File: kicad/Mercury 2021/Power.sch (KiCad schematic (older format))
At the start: 27 parts, among them J1 Batt_Power, J10 3.3v rail, J11 Screw_Terminal_01x02, J12 Screw_Terminal_01x02, J13 Screw_Terminal_01x02, J14 Screw_Terminal_01x02, J2 Screw_Terminal_01x02, J3 Screw_Terminal_01x02, J30 Screw_Terminal_01x02, J31 Screw_Terminal_01x02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

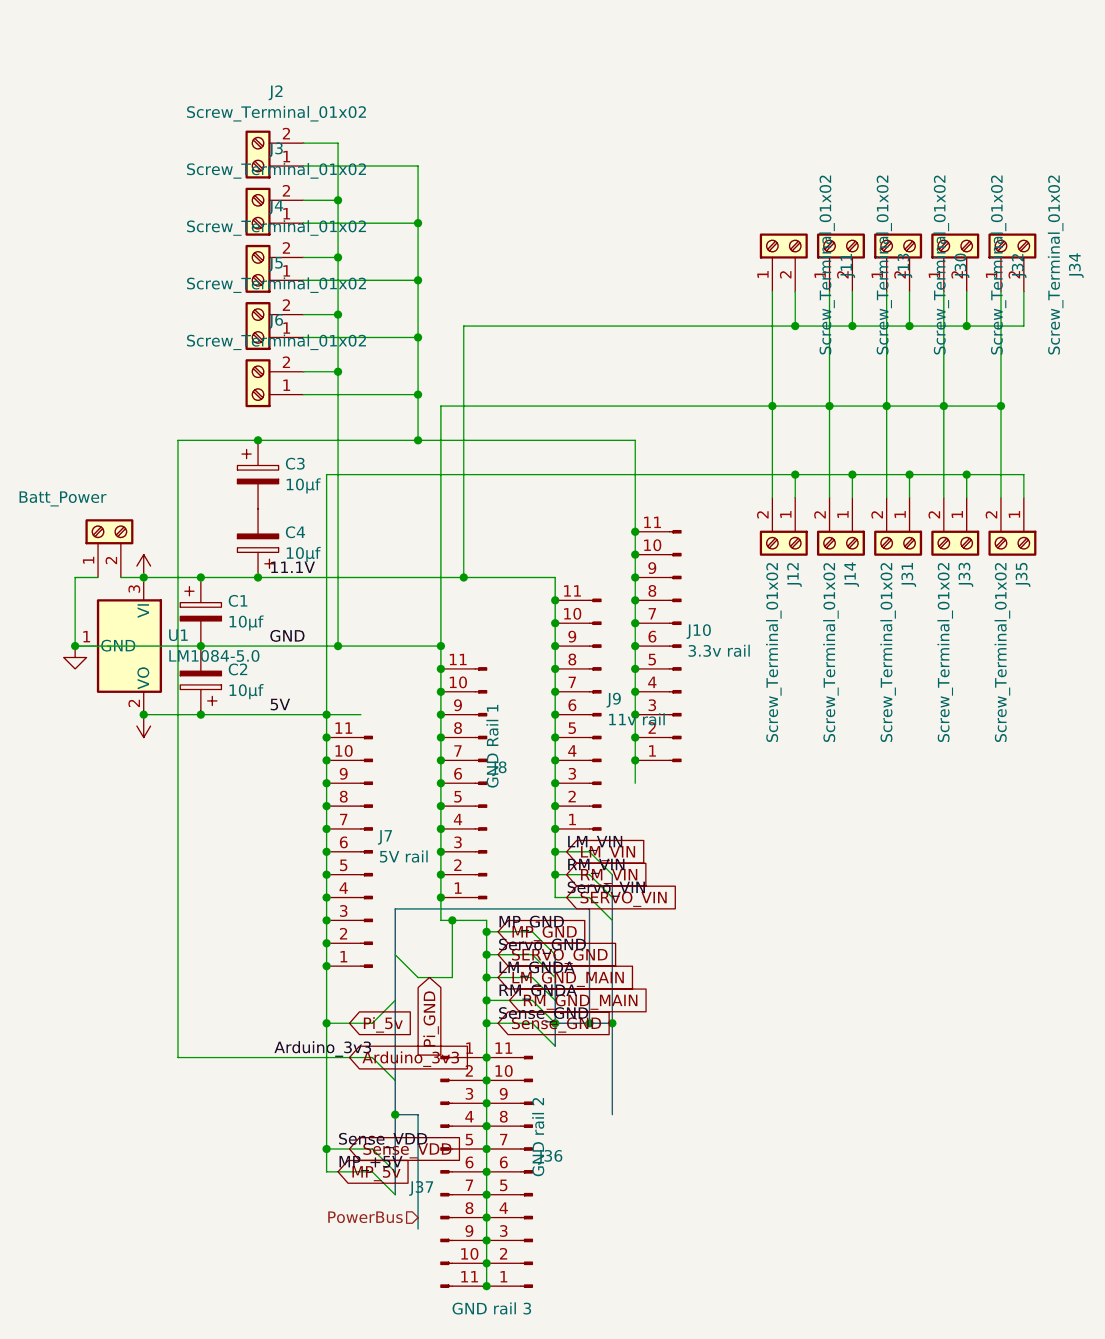
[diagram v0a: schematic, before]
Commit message: Updated new board
- Did PCB traces
-- almost got away with just 2 copper layers, pi ruined it when there was only a bit to go. Probably possible but would take a lot of back and forth
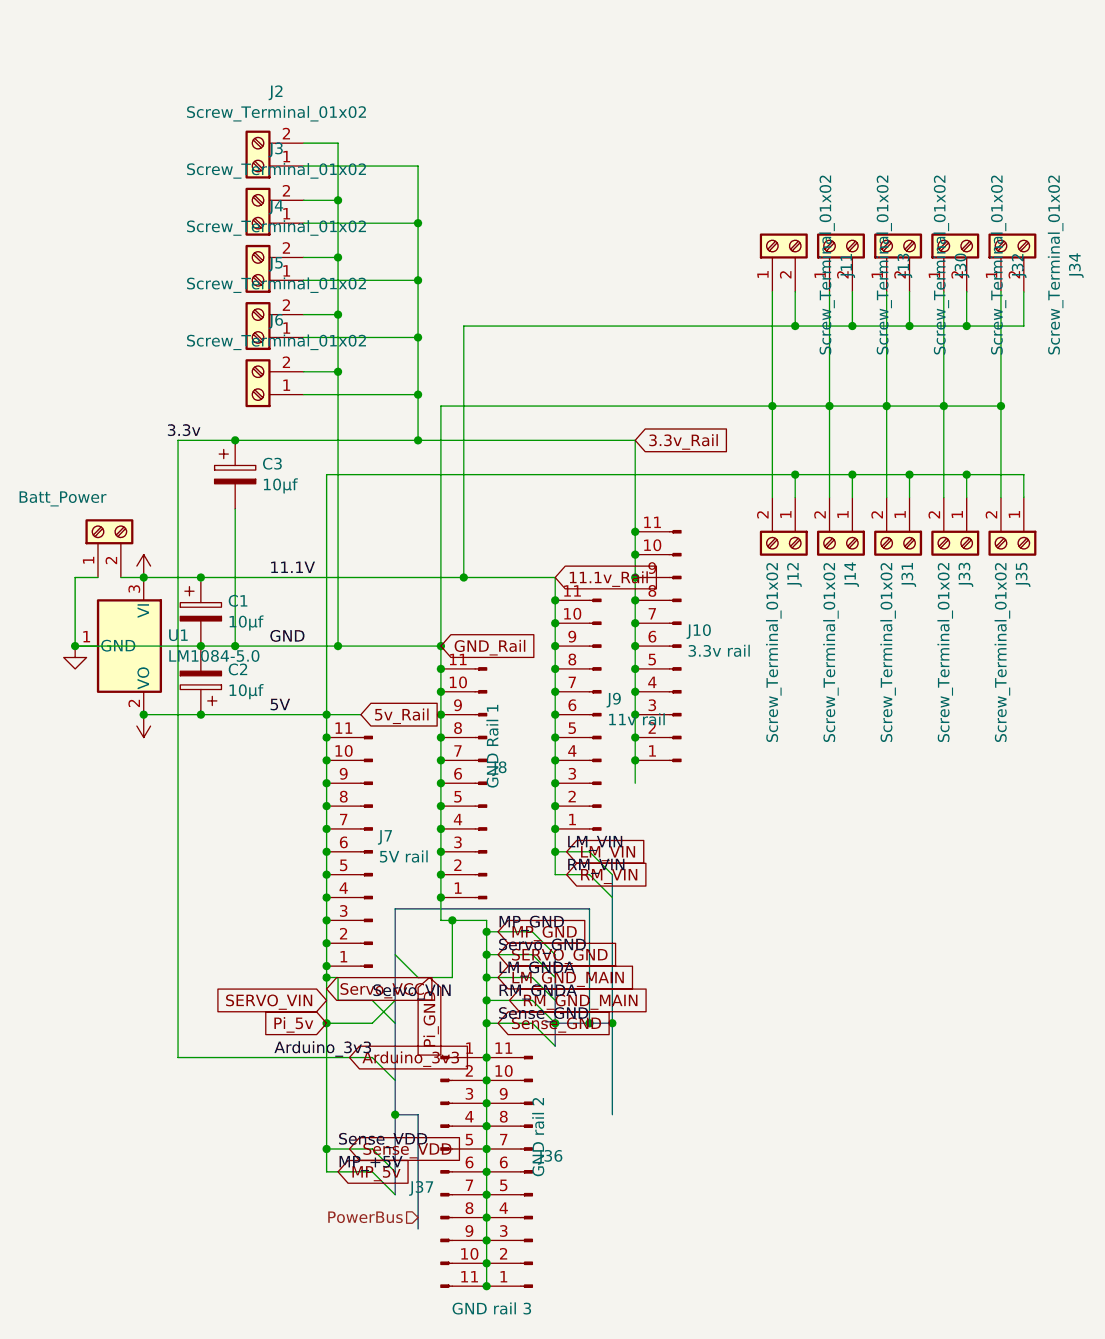
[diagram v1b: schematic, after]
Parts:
- removed C4: 10μf, Capacitor_THT:CP_Radial_D10.0mm_P2.50mm, symbol Device:CP
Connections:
- net GND: now also C3.2
- net Arduino_3v3 renamed 3.3v_Rail
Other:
- moved on the sheet: C3
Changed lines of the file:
@@
 Connection ~ 3450 3850
 Wire Wire Line
-	3450 3850 4050 3850
+	3450 3850 3600 3850
 $Comp
 L Connector:Screw_Terminal_01x02 J?
@@
 	5150 4850 5250 4950
 Entry Wire Line
-	5150 4950 5250 5050
+	4200 5400 4300 5500
 Wire Wire Line
 	5000 4850 5150 4850
 Wire Wire Line
-	5000 4950 5150 4950
+	4050 5400 4200 5400
 Wire Wire Line
 	5000 4750 5150 4750
 Text Label 5050 4850 0    50   ~ 0
 RM_VIN
-Text Label 5050 4950 0    50   ~ 0
-Servo_VIN
 Text Label 5050 4750 0    50   ~ 0
 LM_VIN
@@
 	5000 4750 5000 4850
 Wire Wire Line
-	5000 4850 5000 4950
-Connection ~ 5000 4850
+	4050 5300 4050 5400
 Wire Bus Line
 	4400 6400 4400 5900
@@
 	-1   0    0    1
 $EndComp
-Wire Wire Line
-	3450 3550 3700 3550
-$Comp
-L Device:CP C?
-U 1 1 60EA6068
-P 3700 3400
-AR Path="/60EA6068" Ref="C?"  Part="1"
-AR Path="/60E98AAB/60EA6068" Ref="C4"  Part="1"
-F 0 "C4" H 3582 3354 50  0000 R CNN
-F 1 "10μf" H 3582 3445 50  0000 R CNN
-F 2 "Capacitor_THT:CP_Radial_D10.0mm_P2.50mm" H 3738 3250 50  0001 C CNN
-F 3 "~" H 3700 3400 50  0001 C CNN
-	1    3700 3400
-	-1   0    0    1
-$EndComp
 $Comp
 L Device:CP C?
 U 1 1 60EA606E
-P 3700 3100
+P 3600 3100
 AR Path="/60EA606E" Ref="C?"  Part="1"
 AR Path="/60E98AAB/60EA606E" Ref="C3"  Part="1"
-F 0 "C3" H 3818 3146 50  0000 L CNN
-F 1 "10μf" H 3818 3055 50  0000 L CNN
-F 2 "Capacitor_THT:CP_Radial_D10.0mm_P2.50mm" H 3738 2950 50  0001 C CNN
-F 3 "~" H 3700 3100 50  0001 C CNN
-	1    3700 3100
+F 0 "C3" H 3718 3146 50  0000 L CNN
+F 1 "10μf" H 3718 3055 50  0000 L CNN
+F 2 "Capacitor_THT:CP_Radial_D10.0mm_P2.50mm" H 3638 2950 50  0001 C CNN
+F 3 "~" H 3600 3100 50  0001 C CNN
+	1    3600 3100
 	1    0    0    -1
 $EndComp
@@
 Wire Wire Line
 	3450 4150 4000 4150
-Connection ~ 3700 3550
-Wire Wire Line
-	3700 3550 4600 3550
-Wire Wire Line
-	3350 2950 3700 2950
-Connection ~ 3700 2950
+Wire Wire Line
+	3350 2950 3600 2950
 Connection ~ 5350 3650
 $Comp
@@
 Connection ~ 4400 2950
 Connection ~ 4050 3850
-Wire Wire Line
-	3700 2950 4400 2950
 Wire Wire Line
 	4050 2650 4050 3850
@@
 Text GLabel 5050 4850 2    50   Input ~ 0
 RM_VIN
-Text GLabel 5050 4950 2    50   Input ~ 0
+Text GLabel 4000 5400 0    50   Input ~ 0
 SERVO_VIN
 Text GLabel 4100 6050 2    50   Input ~ 0
@@
 MP_5v
 Wire Wire Line
-	4000 5250 4000 5500
+	4000 5250 4000 5300
 Text GLabel 4100 5650 2    50   Input ~ 0
 Arduino_3v3
-Text GLabel 4100 5500 2    50   Input ~ 0
+Text GLabel 4000 5500 0    50   Input ~ 0
 Pi_5v
 Text GLabel 4450 5300 3    50   Input ~ 0
@@
 Wire Wire Line
 	4550 5300 4400 5300
+Connection ~ 4550 5050
+Wire Wire Line
+	4550 5050 4700 5050
+Text Label 3450 2950 2    50   ~ 0
+3.3v
+Text GLabel 5350 2950 2    50   Input ~ 0
+3.3v_Rail
+Text GLabel 5000 3550 2    50   Input ~ 0
+11.1v_Rail
+Text GLabel 4500 3850 2    50   Input ~ 0
+GND_Rail
+Text GLabel 4150 4150 2    50   Input ~ 0
+5v_Rail
+Connection ~ 3600 2950
+Wire Wire Line
+	3600 3250 3600 3850
+Wire Wire Line
+	3600 2950 4400 2950
+Connection ~ 3600 3850
+Wire Wire Line
+	3600 3850 4050 3850
+Wire Wire Line
+	3450 3550 4600 3550
+Text GLabel 4000 5350 2    50   Input ~ 0
+Servo_VCC
+Text Label 4200 5400 0    50   ~ 0
+Servo_VIN
+Wire Wire Line
+	4050 5300 4000 5300
 Wire Bus Line
 	4300 5900 4300 6250
@@
 Wire Bus Line
 	4300 5000 4300 5900
-Connection ~ 4550 5050
-Wire Wire Line
-	4550 5050 4700 5050
+Connection ~ 4000 5300
+Wire Wire Line
+	4000 5300 4000 5500
 $EndSCHEMATC

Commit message: New New board
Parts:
- removed C3: 10μf, Capacitor_THT:CP_Radial_D10.0mm_P2.50mm, symbol Device:CP
- removed J11, J12, J2, J3, J34, J35, J6: Screw_Terminal_01x02, TerminalBlock:TerminalBlock_Altech_AK300-2_P5.00mm, symbol Connector:Screw_Terminal_01x02
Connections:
- wire segments 162 -> 139
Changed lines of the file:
@@
-$Comp
-L Connector:Screw_Terminal_01x02 J?
-U 1 1 60EA5FEE
-P 6050 3400
-AR Path="/60EA5FEE" Ref="J?"  Part="1"
-AR Path="/60E98AAB/60EA5FEE" Ref="J12"  Part="1"
-F 0 "J12" H 6130 3392 50  0000 L CNN
-F 1 "Screw_Terminal_01x02" H 6130 3301 50  0000 L CNN
-F 2 "TerminalBlock:TerminalBlock_Altech_AK300-2_P5.00mm" H 6050 3400 50  0001 C CNN
-F 3 "~" H 6050 3400 50  0001 C CNN
-	1    6050 3400
-	0    1    1    0
-$EndComp
 $Comp
 L Connector:Screw_Terminal_01x02 J?
@@
 $Comp
 L Connector:Screw_Terminal_01x02 J?
-U 1 1 60EA6006
-P 7050 3400
-AR Path="/60EA6006" Ref="J?"  Part="1"
-AR Path="/60E98AAB/60EA6006" Ref="J35"  Part="1"
-F 0 "J35" H 7130 3392 50  0000 L CNN
-F 1 "Screw_Terminal_01x02" H 7130 3301 50  0000 L CNN
-F 2 "TerminalBlock:TerminalBlock_Altech_AK300-2_P5.00mm" H 7050 3400 50  0001 C CNN
-F 3 "~" H 7050 3400 50  0001 C CNN
-	1    7050 3400
-	0    1    1    0
-$EndComp
-$Comp
-L Connector:Screw_Terminal_01x02 J?
-U 1 1 60EA600C
-P 6950 2100
-AR Path="/60EA600C" Ref="J?"  Part="1"
-AR Path="/60E98AAB/60EA600C" Ref="J34"  Part="1"
-F 0 "J34" H 6868 1775 50  0000 C CNN
-F 1 "Screw_Terminal_01x02" H 6868 1866 50  0000 C CNN
-F 2 "TerminalBlock:TerminalBlock_Altech_AK300-2_P5.00mm" H 6950 2100 50  0001 C CNN
-F 3 "~" H 6950 2100 50  0001 C CNN
-	1    6950 2100
-	0    -1   -1   0
-$EndComp
-$Comp
-L Connector:Screw_Terminal_01x02 J?
 U 1 1 60EA6012
 P 6700 2100
@@
 AR Path="/60E98AAB/60EA6012" Ref="J32"  Part="1"
 F 0 "J32" H 6618 1775 50  0000 C CNN
-F 1 "Screw_Terminal_01x02" H 6618 1866 50  0000 C CNN
+F 1 "Screw_Terminal_01x02" H 7050 1900 50  0000 C CNN
 F 2 "TerminalBlock:TerminalBlock_Altech_AK300-2_P5.00mm" H 6700 2100 50  0001 C CNN
 F 3 "~" H 6700 2100 50  0001 C CNN
@@
 AR Path="/60E98AAB/60EA6018" Ref="J30"  Part="1"
 F 0 "J30" H 6368 1775 50  0000 C CNN
-F 1 "Screw_Terminal_01x02" H 6368 1866 50  0000 C CNN
+F 1 "Screw_Terminal_01x02" H 6950 1850 50  0000 C CNN
 F 2 "TerminalBlock:TerminalBlock_Altech_AK300-2_P5.00mm" H 6450 2100 50  0001 C CNN
 F 3 "~" H 6450 2100 50  0001 C CNN
 	1    6450 2100
-	0    -1   -1   0
-$EndComp
-$Comp
-L Connector:Screw_Terminal_01x02 J?
-U 1 1 60EA601E
-P 6200 2100
-AR Path="/60EA601E" Ref="J?"  Part="1"
-AR Path="/60E98AAB/60EA601E" Ref="J13"  Part="1"
-F 0 "J13" H 6118 1775 50  0000 C CNN
-F 1 "Screw_Terminal_01x02" H 6118 1866 50  0000 C CNN
-F 2 "TerminalBlock:TerminalBlock_Altech_AK300-2_P5.00mm" H 6200 2100 50  0001 C CNN
-F 3 "~" H 6200 2100 50  0001 C CNN
-	1    6200 2100
-	0    -1   -1   0
-$EndComp
-$Comp
-L Connector:Screw_Terminal_01x02 J?
-U 1 1 60EA6024
-P 5950 2100
-AR Path="/60EA6024" Ref="J?"  Part="1"
-AR Path="/60E98AAB/60EA6024" Ref="J11"  Part="1"
-F 0 "J11" H 5868 1775 50  0000 C CNN
-F 1 "Screw_Terminal_01x02" H 5868 1866 50  0000 C CNN
-F 2 "TerminalBlock:TerminalBlock_Altech_AK300-2_P5.00mm" H 5950 2100 50  0001 C CNN
-F 3 "~" H 5950 2100 50  0001 C CNN
-	1    5950 2100
 	0    -1   -1   0
 $EndComp
@@
 	-1   0    0    1
 $EndComp
-$Comp
-L Device:CP C?
-U 1 1 60EA606E
-P 3600 3100
-AR Path="/60EA606E" Ref="C?"  Part="1"
-AR Path="/60E98AAB/60EA606E" Ref="C3"  Part="1"
-F 0 "C3" H 3718 3146 50  0000 L CNN
-F 1 "10μf" H 3718 3055 50  0000 L CNN
-F 2 "Capacitor_THT:CP_Radial_D10.0mm_P2.50mm" H 3638 2950 50  0001 C CNN
-F 3 "~" H 3600 3100 50  0001 C CNN
-	1    3600 3100
-	1    0    0    -1
-$EndComp
 Wire Wire Line
 	3200 4150 3450 4150
@@
 Wire Wire Line
 	3450 4150 4000 4150
-Wire Wire Line
-	3350 2950 3600 2950
 Connection ~ 5350 3650
-$Comp
-L Connector:Screw_Terminal_01x02 J?
-U 1 1 60EA60A0
-P 3700 1750
-AR Path="/60EA60A0" Ref="J?"  Part="1"
-AR Path="/60E98AAB/60EA60A0" Ref="J2"  Part="1"
-F 0 "J2" H 3618 1425 50  0000 C CNN
-F 1 "Screw_Terminal_01x02" H 3618 1516 50  0000 C CNN
-F 2 "TerminalBlock:TerminalBlock_Altech_AK300-2_P5.00mm" H 3700 1750 50  0001 C CNN
-F 3 "~" H 3700 1750 50  0001 C CNN
-	1    3700 1750
-	-1   0    0    1
-$EndComp
-$Comp
-L Connector:Screw_Terminal_01x02 J?
-U 1 1 60EA60A6
-P 3700 2000
-AR Path="/60EA60A6" Ref="J?"  Part="1"
-AR Path="/60E98AAB/60EA60A6" Ref="J3"  Part="1"
-F 0 "J3" H 3618 1675 50  0000 C CNN
-F 1 "Screw_Terminal_01x02" H 3618 1766 50  0000 C CNN
-F 2 "TerminalBlock:TerminalBlock_Altech_AK300-2_P5.00mm" H 3700 2000 50  0001 C CNN
-F 3 "~" H 3700 2000 50  0001 C CNN
-	1    3700 2000
-	-1   0    0    1
-$EndComp
-$Comp
-L Connector:Screw_Terminal_01x02 J?
-U 1 1 60EA60AC
-P 3700 2250
-AR Path="/60EA60AC" Ref="J?"  Part="1"
-AR Path="/60E98AAB/60EA60AC" Ref="J4"  Part="1"
-F 0 "J4" H 3618 1925 50  0000 C CNN
-F 1 "Screw_Terminal_01x02" H 3618 2016 50  0000 C CNN
-F 2 "TerminalBlock:TerminalBlock_Altech_AK300-2_P5.00mm" H 3700 2250 50  0001 C CNN
-F 3 "~" H 3700 2250 50  0001 C CNN
-	1    3700 2250
-	-1   0    0    1
-$EndComp
-$Comp
-L Connector:Screw_Terminal_01x02 J?
-U 1 1 60EA60B2
-P 3700 2500
-AR Path="/60EA60B2" Ref="J?"  Part="1"
-AR Path="/60E98AAB/60EA60B2" Ref="J5"  Part="1"
-F 0 "J5" H 3618 2175 50  0000 C CNN
-F 1 "Screw_Terminal_01x02" H 3618 2266 50  0000 C CNN
-F 2 "TerminalBlock:TerminalBlock_Altech_AK300-2_P5.00mm" H 3700 2500 50  0001 C CNN
-F 3 "~" H 3700 2500 50  0001 C CNN
-	1    3700 2500
-	-1   0    0    1
-$EndComp
-$Comp
-L Connector:Screw_Terminal_01x02 J?
-U 1 1 60EA60B8
-P 3700 2750
-AR Path="/60EA60B8" Ref="J?"  Part="1"
-AR Path="/60E98AAB/60EA60B8" Ref="J6"  Part="1"
-F 0 "J6" H 3618 2425 50  0000 C CNN
-F 1 "Screw_Terminal_01x02" H 3618 2516 50  0000 C CNN
-F 2 "TerminalBlock:TerminalBlock_Altech_AK300-2_P5.00mm" H 3700 2750 50  0001 C CNN
-F 3 "~" H 3700 2750 50  0001 C CNN
-	1    3700 2750
-	-1   0    0    1
-$EndComp
-Wire Wire Line
-	4050 1650 3900 1650
-Wire Wire Line
-	3900 1900 4050 1900
-Connection ~ 4050 1900
-Wire Wire Line
-	4050 1900 4050 1650
-Wire Wire Line
-	3900 2150 4050 2150
-Connection ~ 4050 2150
-Wire Wire Line
-	4050 2150 4050 1900
-Wire Wire Line
-	3900 2400 4050 2400
-Connection ~ 4050 2400
-Wire Wire Line
-	4050 2400 4050 2150
-Wire Wire Line
-	3900 2650 4050 2650
-Connection ~ 4050 2650
-Wire Wire Line
-	4050 2650 4050 2400
-Wire Wire Line
-	4400 1750 3900 1750
-Wire Wire Line
-	3900 2000 4400 2000
-Connection ~ 4400 2000
-Wire Wire Line
-	4400 2000 4400 1750
-Wire Wire Line
-	3900 2250 4400 2250
-Connection ~ 4400 2250
-Wire Wire Line
-	4400 2250 4400 2000
-Wire Wire Line
-	3900 2500 4400 2500
-Connection ~ 4400 2500
-Wire Wire Line
-	4400 2500 4400 2250
-Wire Wire Line
-	3900 2750 4400 2750
-Connection ~ 4400 2750
-Wire Wire Line
-	4400 2750 4400 2500
-Wire Wire Line
-	4400 2750 4400 2950
-Connection ~ 4400 2950
-Connection ~ 4050 3850
-Wire Wire Line
-	4050 2650 4050 3850
-Wire Wire Line
-	4050 3850 4500 3850
 Wire Wire Line
 	4500 2800 4500 3850
@@
 Wire Wire Line
 	4600 3550 5000 3550
-Wire Wire Line
-	4400 2950 5350 2950
 Wire Wire Line
 	4600 2450 4600 3550
@@
 Text GLabel 4150 4150 2    50   Input ~ 0
 5v_Rail
-Connection ~ 3600 2950
 Wire Wire Line
 	3600 3250 3600 3850
-Wire Wire Line
-	3600 2950 4400 2950
 Connection ~ 3600 3850
-Wire Wire Line
-	3600 3850 4050 3850
 Wire Wire Line
 	3450 3550 4600 3550
@@
 Wire Wire Line
 	4050 5300 4000 5300
+Connection ~ 4000 5300
+Wire Wire Line
+	4000 5300 4000 5500
+Wire Wire Line
+	3600 3850 4500 3850
+Wire Wire Line
+	3350 2950 5350 2950
+$Comp
+L Connector:Screw_Terminal_01x02 J?
+U 1 1 60EA601E
+P 6200 2100
+AR Path="/60EA601E" Ref="J?"  Part="1"
+AR Path="/60E98AAB/60EA601E" Ref="J13"  Part="1"
+F 0 "J13" H 6118 1775 50  0000 C CNN
+F 1 "Screw_Terminal_01x02" H 6118 1866 50  0000 C CNN
+F 2 "TerminalBlock:TerminalBlock_Altech_AK300-2_P5.00mm" H 6200 2100 50  0001 C CNN
+F 3 "~" H 6200 2100 50  0001 C CNN
+	1    6200 2100
+	0    -1   -1   0
+$EndComp
+$Comp
+L Connector:Screw_Terminal_01x02 J?
+U 1 1 609BEEEE
+P 6050 3400
+AR Path="/609BEEEE" Ref="J?"  Part="1"
+AR Path="/60E98AAB/609BEEEE" Ref="J5"  Part="1"
+F 0 "J5" H 6130 3392 50  0000 L CNN
+F 1 "Screw_Terminal_01x02" H 6130 3301 50  0000 L CNN
+F 2 "TerminalBlock:TerminalBlock_Altech_AK300-2_P5.00mm" H 6050 3400 50  0001 C CNN
+F 3 "~" H 6050 3400 50  0001 C CNN
+	1    6050 3400
+	0    1    1    0
+$EndComp
+$Comp
+L Connector:Screw_Terminal_01x02 J?
+U 1 1 609C503B
+P 5950 2100
+AR Path="/609C503B" Ref="J?"  Part="1"
+AR Path="/60E98AAB/609C503B" Ref="J4"  Part="1"
+F 0 "J4" H 5868 1775 50  0000 C CNN
+F 1 "Screw_Terminal_01x02" H 5868 1866 50  0000 C CNN
+F 2 "TerminalBlock:TerminalBlock_Altech_AK300-2_P5.00mm" H 5950 2100 50  0001 C CNN
+F 3 "~" H 5950 2100 50  0001 C CNN
+	1    5950 2100
+	0    -1   -1   0
+$EndComp
 Wire Bus Line
 	4300 5900 4300 6250
@@
 Wire Bus Line
 	4300 5000 4300 5900
-Connection ~ 4000 5300
-Wire Wire Line
-	4000 5300 4000 5500
 $EndSCHEMATC

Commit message: NOTE! Updated PCB
This is different than the PCBs that were ordered.
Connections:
- wire segments 139 -> 137
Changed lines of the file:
@@
 Connection ~ 3450 3550
 Connection ~ 3450 3850
-Wire Wire Line
-	3450 3850 3600 3850
 $Comp
 L Connector:Screw_Terminal_01x02 J?
@@
 5v_Rail
 Wire Wire Line
-	3600 3250 3600 3850
-Connection ~ 3600 3850
-Wire Wire Line
 	3450 3550 4600 3550
 Text GLabel 4000 5350 2    50   Input ~ 0
@@
 Wire Wire Line
 	4000 5300 4000 5500
-Wire Wire Line
-	3600 3850 4500 3850
 Wire Wire Line
 	3350 2950 5350 2950
@@
 Wire Bus Line
 	4300 5000 4300 5900
+Wire Wire Line
+	3450 3850 4500 3850
 $EndSCHEMATC

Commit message: Updated PCB
Updated Labels & arduino now powered off of board.
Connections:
- net labels added: Arduino_VIN
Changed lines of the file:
@@
 	0    -1   -1   0
 $EndComp
+Wire Wire Line
+	3450 3850 4500 3850
 Wire Bus Line
 	4300 5900 4300 6250
@@
 Wire Bus Line
 	4300 5000 4300 5900
-Wire Wire Line
-	3450 3850 4500 3850
+Text GLabel 4000 4000 2    50   Input ~ 0
+Arduino_VIN
 $EndSCHEMATC
